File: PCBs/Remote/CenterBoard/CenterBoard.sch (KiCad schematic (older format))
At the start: 4 parts, among them U101 Sparkfun_COM-09032, U102 Sparkfun_COM-09032

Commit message: Bezig met LEDS
Signed-off-by: Eldalote.Electronics <Eldalote.Electronics@gmail.com>
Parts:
- renumbered LOGO1 to LOGO101
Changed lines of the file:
@@
 $Descr A4 11693 8268
 encoding utf-8
-Sheet 1 4
+Sheet 1 5
 Title ""
 Date ""
@@
 $EndDescr
 $Comp
-L Graphic:Logo_Open_Hardware_Small LOGO1
+L Graphic:Logo_Open_Hardware_Small LOGO101
 U 1 1 5F436516
 P 4050 7550
-F 0 "LOGO1" H 4050 7825 50  0001 C CNN
+F 0 "LOGO101" H 4050 7825 50  0001 C CNN
 F 1 "Logo_Open_Hardware_Small" H 4050 7325 50  0001 C CNN
 F 2 "Symbol:OSHW-Logo_5.7x6mm_SilkScreen" H 4050 7550 50  0001 C CNN
@@
 	1    0    0    -1
 $EndComp
+$Sheet
+S 12000 3500 500  500
+U 5FAB246F
+F0 "LEDs and Screen" 50
+F1 "LEDs-screen.sch" 50
+$EndSheet
 $EndSCHEMATC

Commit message: Continued work with the center board
Signed-off-by: Eldalote.Electronics <Eldalote.Electronics@gmail.com>
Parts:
- removed R101: PTA6043, Eldalote-footprints:PTA6043, symbol Eldalote-General:PTA6043
- removed U101, U102: Sparkfun_COM-09032, Eldalote-footprints:Sparkfun_COM-09032, symbol Eldalote-General:Sparkfun_COM-09032
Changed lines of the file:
@@
 $Descr A4 11693 8268
 encoding utf-8
-Sheet 1 5
+Sheet 1 6
 Title ""
 Date ""
@@
 F1 "Radio.sch" 50
 $EndSheet
-$Comp
-L Eldalote-General:PTA6043 R101
-U 1 1 5FA79FE9
-P 10100 5650
-F 0 "R101" H 9907 5446 50  0000 R CNN
-F 1 "PTA6043" H 9907 5355 50  0000 R CNN
-F 2 "Eldalote-footprints:PTA6043" H 10100 5650 50  0001 C CNN
-F 3 "" H 10100 5650 50  0001 C CNN
-	1    10100 5650
-	1    0    0    -1
-$EndComp
-$Comp
-L Eldalote-General:Sparkfun_COM-09032 U101
-U 1 1 5FA7B340
-P 8500 5250
-F 0 "U101" H 8830 5246 50  0000 L CNN
-F 1 "Sparkfun_COM-09032" H 8830 5155 50  0000 L CNN
-F 2 "Eldalote-footprints:Sparkfun_COM-09032" H 8500 5250 50  0001 L BNN
-F 3 "" H 8500 5250 50  0001 L BNN
-	1    8500 5250
-	1    0    0    -1
-$EndComp
-$Comp
-L Eldalote-General:Sparkfun_COM-09032 U102
-U 1 1 5FA7B424
-P 10100 4450
-F 0 "U102" H 10430 4446 50  0000 L CNN
-F 1 "Sparkfun_COM-09032" H 10430 4355 50  0000 L CNN
-F 2 "Eldalote-footprints:Sparkfun_COM-09032" H 10100 4450 50  0001 L BNN
-F 3 "" H 10100 4450 50  0001 L BNN
-	1    10100 4450
-	1    0    0    -1
-$EndComp
 $Sheet
 S 12000 3500 500  500
@@
 F1 "LEDs-screen.sch" 50
 $EndSheet
+$Sheet
+S 12000 4500 500  500
+U 5FB8F5C2
+F0 "Joysticks and Throttle" 50
+F1 "joysticks-throttle.sch" 50
+$EndSheet
 $EndSCHEMATC

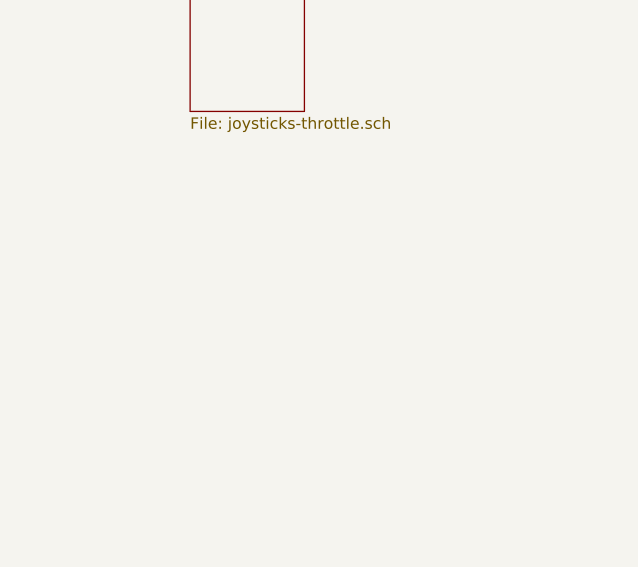
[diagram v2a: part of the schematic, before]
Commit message: Made the keyboard PCB. With LPC software started pin assignment on the LPC
Signed-off-by: Eldalote.Electronics <Eldalote.Electronics@gmail.com>
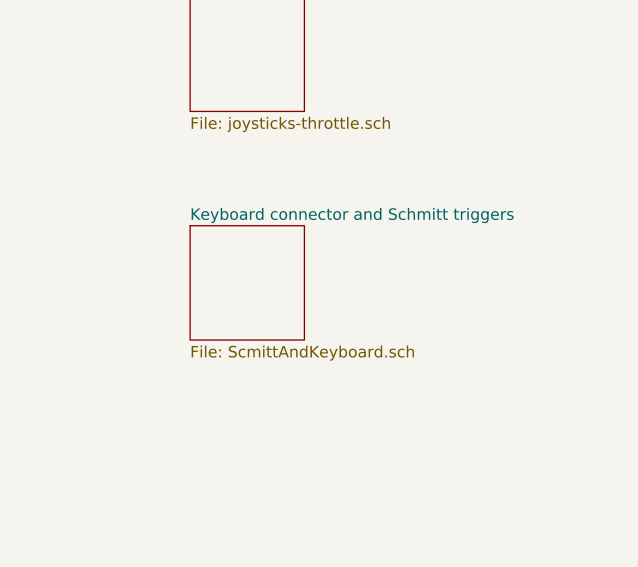
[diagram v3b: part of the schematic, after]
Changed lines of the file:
@@
 $Descr A4 11693 8268
 encoding utf-8
-Sheet 1 6
+Sheet 1 7
 Title ""
 Date ""
@@
 $Comp
 L Graphic:Logo_Open_Hardware_Small LOGO101
-U 1 1 5F436516
+U 1 1 5FB80A11
 P 4050 7550
 F 0 "LOGO101" H 4050 7825 50  0001 C CNN
@@
 F1 "joysticks-throttle.sch" 50
 $EndSheet
+$Sheet
+S 12000 5500 500  500
+U 5FB8048A
+F0 "Keyboard connector and Schmitt triggers" 50
+F1 "ScmittAndKeyboard.sch" 50
+$EndSheet
 $EndSCHEMATC

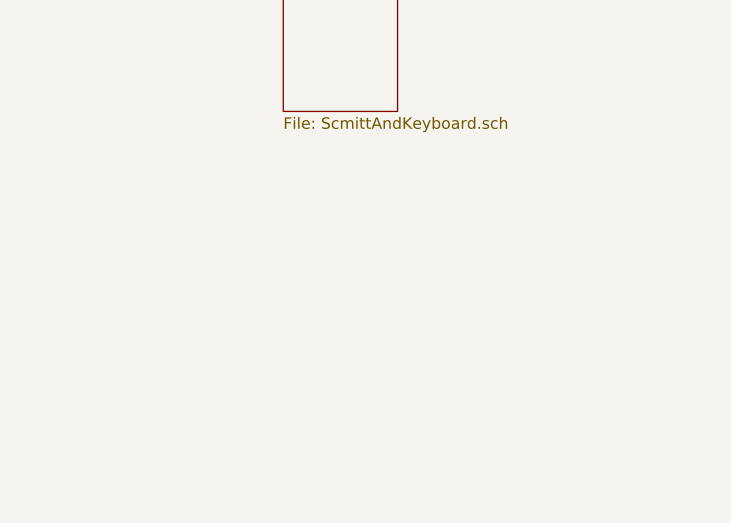
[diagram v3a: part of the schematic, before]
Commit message: Redid the radio PCB layout on both drone and remote PCB. Drone PCB had old schematic, remote PCB layout wasn't ideal.
Copied in the VHDL project files from the seperate VHDL project into the main "All in one" project.

Signed-off-by: Eldalote.Electronics <Eldalote.Electronics@gmail.com>
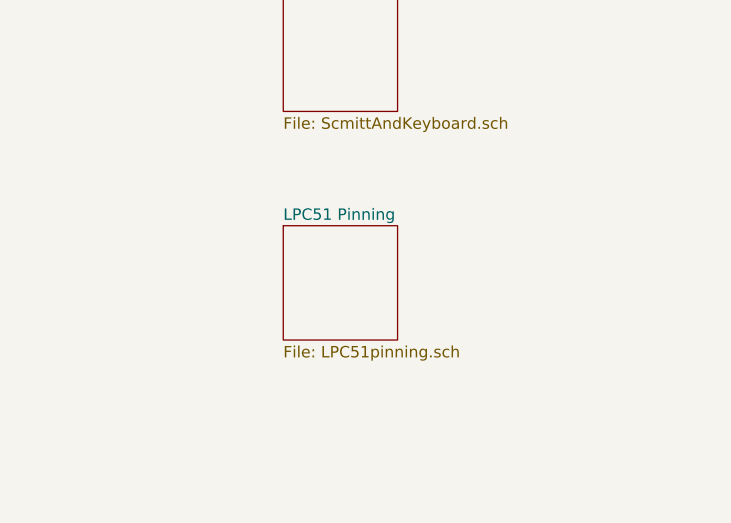
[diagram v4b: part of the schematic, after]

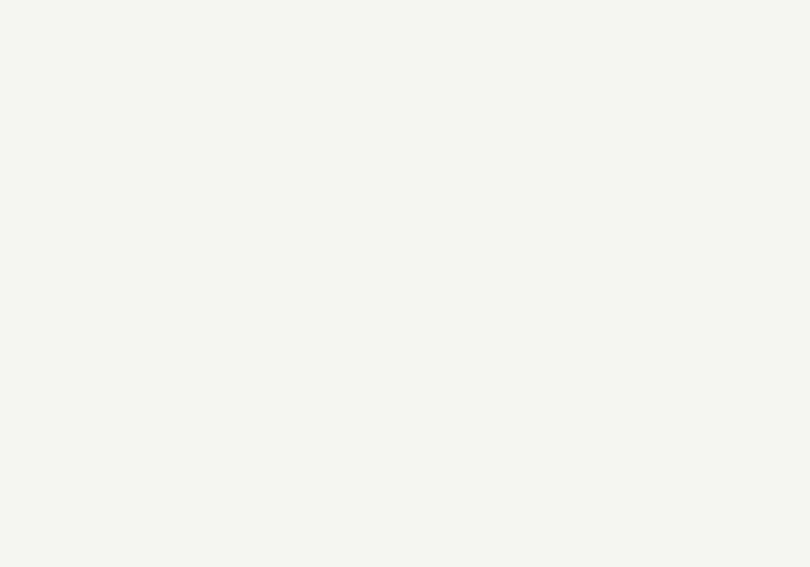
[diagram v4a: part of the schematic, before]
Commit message: Some cleanup, and PCB antenna removal.
Last edits before asking for reddit feedback.

Signed-off-by: Eldalote.Electronics <Eldalote.Electronics@gmail.com>
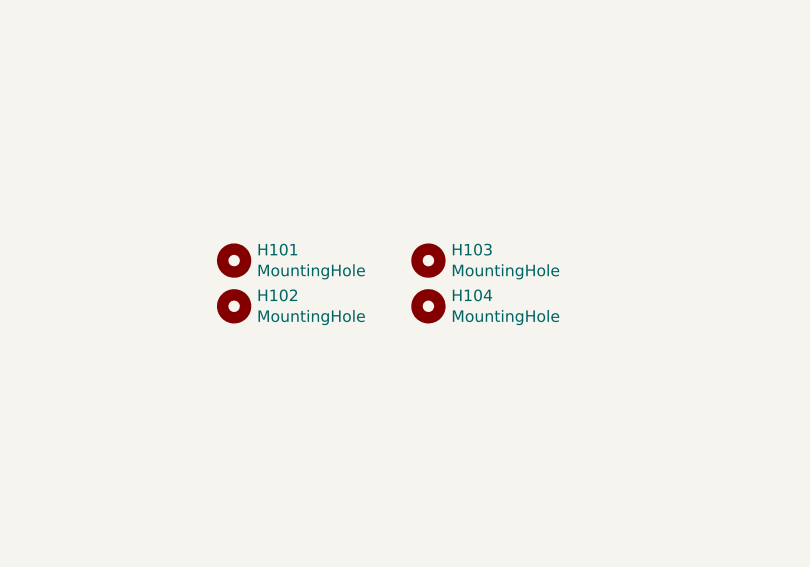
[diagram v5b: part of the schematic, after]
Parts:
- added H101, H102, H103, H104: MountingHole, MountingHole:MountingHole_3.2mm_M3_ISO7380, symbol Mechanical:MountingHole
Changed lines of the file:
@@
 F1 "LPC51pinning.sch" 50
 $EndSheet
+$Comp
+L Mechanical:MountingHole H101
+U 1 1 5FE46077
+P 8100 6100
+F 0 "H101" H 8200 6146 50  0000 L CNN
+F 1 "MountingHole" H 8200 6055 50  0000 L CNN
+F 2 "MountingHole:MountingHole_3.2mm_M3_ISO7380" H 8100 6100 50  0001 C CNN
+F 3 "~" H 8100 6100 50  0001 C CNN
+	1    8100 6100
+	1    0    0    -1
+$EndComp
+$Comp
+L Mechanical:MountingHole H102
+U 1 1 5FE4669B
+P 8100 6300
+F 0 "H102" H 8200 6346 50  0000 L CNN
+F 1 "MountingHole" H 8200 6255 50  0000 L CNN
+F 2 "MountingHole:MountingHole_3.2mm_M3_ISO7380" H 8100 6300 50  0001 C CNN
+F 3 "~" H 8100 6300 50  0001 C CNN
+	1    8100 6300
+	1    0    0    -1
+$EndComp
+$Comp
+L Mechanical:MountingHole H103
+U 1 1 5FE4680B
+P 8950 6100
+F 0 "H103" H 9050 6146 50  0000 L CNN
+F 1 "MountingHole" H 9050 6055 50  0000 L CNN
+F 2 "MountingHole:MountingHole_3.2mm_M3_ISO7380" H 8950 6100 50  0001 C CNN
+F 3 "~" H 8950 6100 50  0001 C CNN
+	1    8950 6100
+	1    0    0    -1
+$EndComp
+$Comp
+L Mechanical:MountingHole H104
+U 1 1 5FE46A60
+P 8950 6300
+F 0 "H104" H 9050 6346 50  0000 L CNN
+F 1 "MountingHole" H 9050 6255 50  0000 L CNN
+F 2 "MountingHole:MountingHole_3.2mm_M3_ISO7380" H 8950 6300 50  0001 C CNN
+F 3 "~" H 8950 6300 50  0001 C CNN
+	1    8950 6300
+	1    0    0    -1
+$EndComp
 $EndSCHEMATC

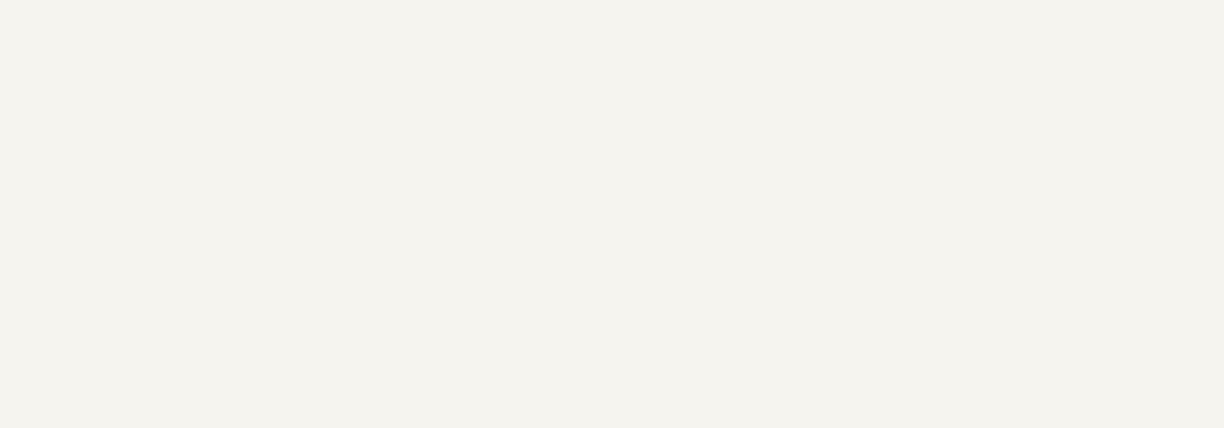
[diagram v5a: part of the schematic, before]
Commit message: Added PDFs of schematics. Corrected a few value labels in drone schematic.
Signed-off-by: Eldalote.Electronics <Eldalote.Electronics@gmail.com>
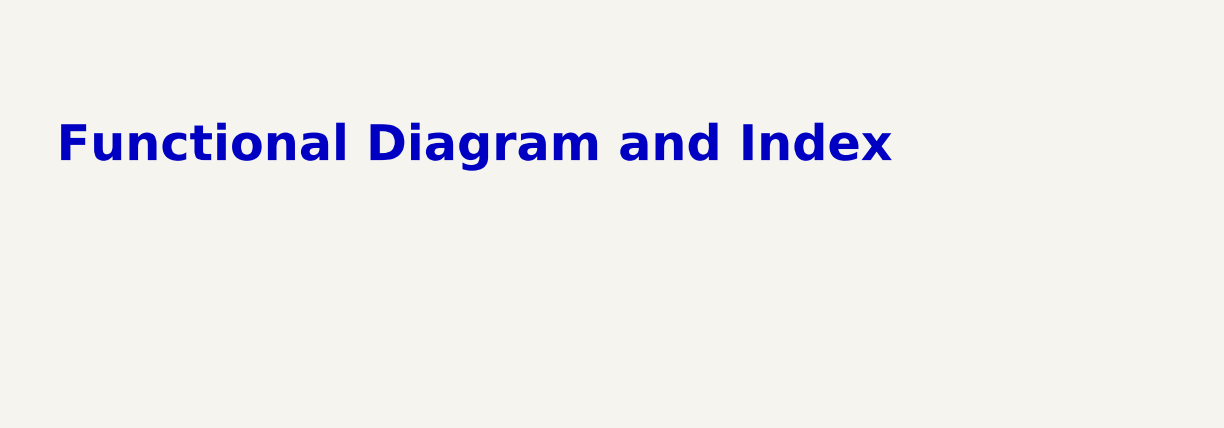
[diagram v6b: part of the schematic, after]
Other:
- note added: "Functional Diagram and Index"
